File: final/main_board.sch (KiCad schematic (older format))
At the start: 55 parts, among them J1 USB_microB_2040002-1, J2 Arduino_ICSP, J3 Conn_01x15_Male, J4 Conn_01x15_Male, J5 E-INK DISPLAY, J6 BT CONFIG, U1 FT232RL, U2 MCP1702T-5002E_CB, U3 TPS2113ADRBR, U4 ATMEGA328PB-ANR, U5 TXS0108EPW, U6 TXS0104E, U7 RN4871, U8 MCP1702T-3302E/CBCT-ND, U9 TS02CQE, Y1 16MHz

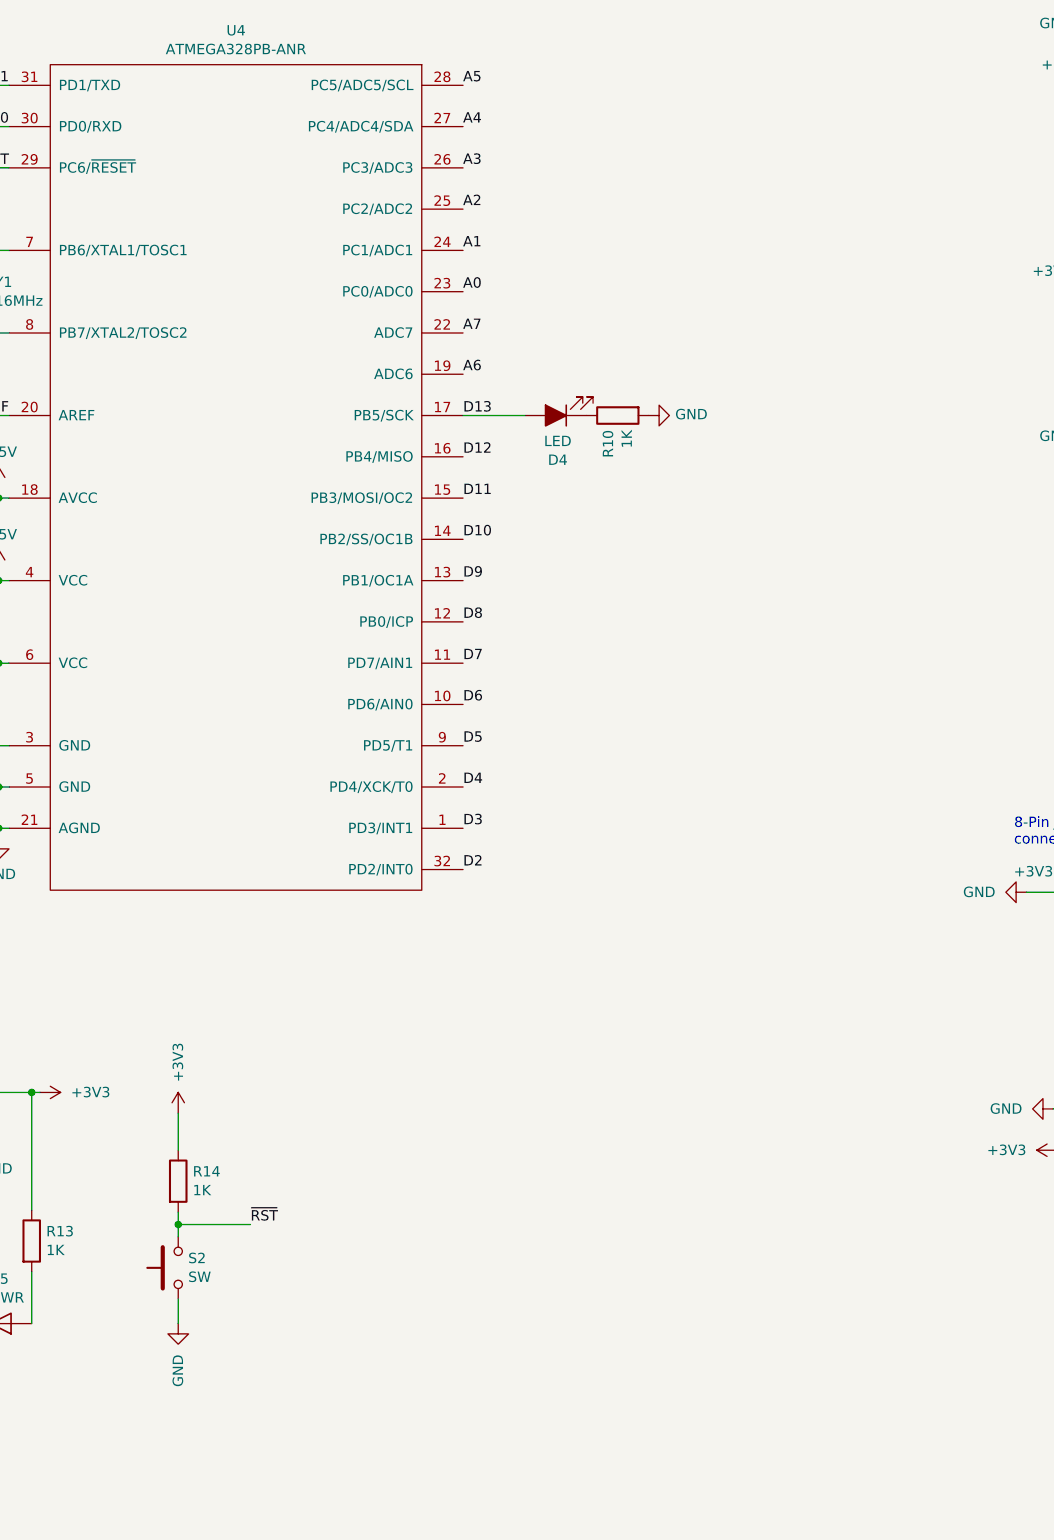
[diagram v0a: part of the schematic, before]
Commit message: Add mode button.
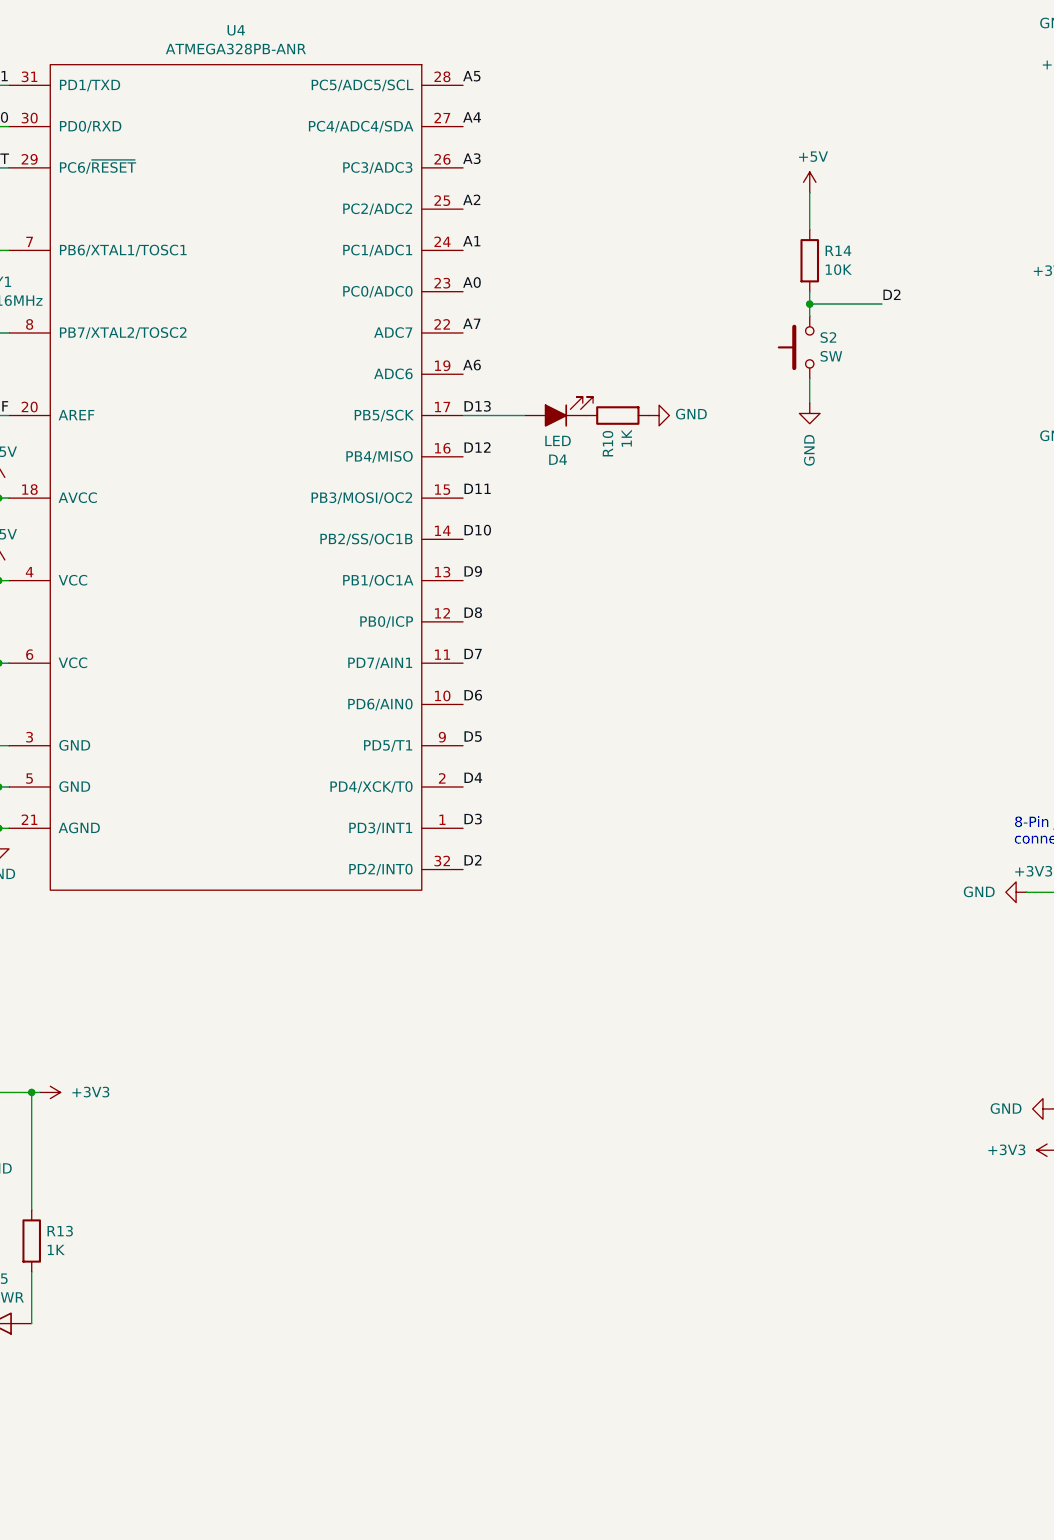
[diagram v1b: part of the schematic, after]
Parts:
- R14: value 1K -> 10K
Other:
- moved on the sheet: R14, S2
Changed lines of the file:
@@
 ~RST
-$Comp
-L power:+3V3 #PWR053
-U 1 1 5CB45D45
-P 9520 9180
-F 0 "#PWR053" H 9520 9030 50  0001 C CNN
-F 1 "+3V3" V 9520 9330 50  0000 L CNN
-F 2 "" H 9520 9180 50  0001 C CNN
-F 3 "" H 9520 9180 50  0001 C CNN
-	1    9520 9180
-	-1   0    0    -1
-$EndComp
 $Comp
 L main_board-rescue:SW-final S2
 U 1 1 5CB4A3A3
-P 9520 9930
-F 0 "S2" H 9568 9976 50  0000 L CNN
-F 1 "SW" H 9568 9885 50  0000 L CNN
-F 2 "Button_Switch_SMD:SW_SPST_B3U-1000P" V 9570 10030 60  0001 C CNN
-F 3 "" V 9570 10030 60  0001 C CNN
-	1    9520 9930
+P 12580 5470
+F 0 "S2" H 12628 5516 50  0000 L CNN
+F 1 "SW" H 12628 5425 50  0000 L CNN
+F 2 "Button_Switch_SMD:SW_SPST_B3U-1000P" V 12630 5570 60  0001 C CNN
+F 3 "" V 12630 5570 60  0001 C CNN
+	1    12580 5470
 	1    0    0    -1
 $EndComp
@@
 L Device:R R14
 U 1 1 5CB4A75B
-P 9520 9510
-F 0 "R14" H 9590 9556 50  0000 L CNN
-F 1 "1K" H 9590 9465 50  0000 L CNN
-F 2 "" V 9450 9510 50  0001 C CNN
-F 3 "~" H 9520 9510 50  0001 C CNN
-	1    9520 9510
+P 12580 5050
+F 0 "R14" H 12650 5096 50  0000 L CNN
+F 1 "10K" H 12650 5005 50  0000 L CNN
+F 2 "" V 12510 5050 50  0001 C CNN
+F 3 "~" H 12580 5050 50  0001 C CNN
+	1    12580 5050
 	1    0    0    -1
 $EndComp
@@
 L power:GND #PWR054
 U 1 1 5CB4A82B
-P 9520 10200
-F 0 "#PWR054" H 9520 9950 50  0001 C CNN
-F 1 "GND" V 9520 10050 50  0000 R CNN
-F 2 "" H 9520 10200 50  0001 C CNN
-F 3 "" H 9520 10200 50  0001 C CNN
-	1    9520 10200
-	1    0    0    -1
-$EndComp
-Wire Wire Line
-	9520 9180 9520 9360
-Wire Wire Line
-	9520 9660 9520 9720
-Wire Wire Line
-	9520 10080 9520 10200
-Text Label 9870 9720 0    50   ~ 0
-~RST
-Wire Wire Line
-	9870 9720 9520 9720
-Connection ~ 9520 9720
-Wire Wire Line
-	9520 9720 9520 9780
+P 12580 5740
+F 0 "#PWR054" H 12580 5490 50  0001 C CNN
+F 1 "GND" V 12580 5590 50  0000 R CNN
+F 2 "" H 12580 5740 50  0001 C CNN
+F 3 "" H 12580 5740 50  0001 C CNN
+	1    12580 5740
+	1    0    0    -1
+$EndComp
+Wire Wire Line
+	12580 4720 12580 4900
+Wire Wire Line
+	12580 5200 12580 5260
+Wire Wire Line
+	12580 5620 12580 5740
+Text Label 12930 5260 0    50   ~ 0
+D2
+Wire Wire Line
+	12930 5260 12580 5260
+Connection ~ 12580 5260
+Wire Wire Line
+	12580 5260 12580 5320
 $Comp
 L Connector:Conn_01x08_Male J6
@@
 Connection ~ 11750 1950
 NoConn ~ 11150 2150
+$Comp
+L power:+5V #PWR?
+U 1 1 5CAC5114
+P 12580 4720
+F 0 "#PWR?" H 12580 4570 50  0001 C CNN
+F 1 "+5V" H 12595 4893 50  0000 C CNN
+F 2 "" H 12580 4720 50  0001 C CNN
+F 3 "" H 12580 4720 50  0001 C CNN
+	1    12580 4720
+	1    0    0    -1
+$EndComp
 $EndSCHEMATC

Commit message: Add diode to 3V3 output of FTDI and power display from Lin Reg.
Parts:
- added D6: D_Schottky, symbol Device:D_Schottky
- added R15: 1K, symbol Device:R
- added S3: SW, Button_Switch_SMD:SW_SPST_B3U-1000P, symbol main_board-rescue:SW-final
- R14: value 10K -> 1K
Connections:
- wire segments 154 -> 159
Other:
- moved on the sheet: R14, S2
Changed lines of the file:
@@
 L power:+3V3 #PWR03
 U 1 1 5C4E2E65
-P 3300 6800
-F 0 "#PWR03" H 3300 6650 50  0001 C CNN
-F 1 "+3V3" V 3315 6928 50  0000 L CNN
-F 2 "" H 3300 6800 50  0001 C CNN
-F 3 "" H 3300 6800 50  0001 C CNN
-	1    3300 6800
+P 3000 6800
+F 0 "#PWR03" H 3000 6650 50  0001 C CNN
+F 1 "+3V3" V 3015 6928 50  0000 L CNN
+F 2 "" H 3000 6800 50  0001 C CNN
+F 3 "" H 3000 6800 50  0001 C CNN
+	1    3000 6800
 	0    -1   -1   0
 $EndComp
@@
 Text Label 14200 5000 2    50   ~ 0
 AREF
-$Comp
-L power:+3V3 #PWR035
-U 1 1 5C5A4A29
-P 13910 8010
-F 0 "#PWR035" H 13910 7860 50  0001 C CNN
-F 1 "+3V3" V 13910 8160 50  0000 L CNN
-F 2 "" H 13910 8010 50  0001 C CNN
-F 3 "" H 13910 8010 50  0001 C CNN
-	1    13910 8010
-	0    -1   1    0
-$EndComp
 Wire Wire Line
 	14000 5100 14200 5100
@@
 	7620 10600 7620 10680
 $Comp
-L power:+3V3 #PWR052
-U 1 1 5CB03E2A
-P 8850 9080
-F 0 "#PWR052" H 8850 8930 50  0001 C CNN
-F 1 "+3V3" V 8850 9230 50  0000 L CNN
-F 2 "" H 8850 9080 50  0001 C CNN
-F 3 "" H 8850 9080 50  0001 C CNN
-	1    8850 9080
-	0    1    -1   0
-$EndComp
-$Comp
 L Device:C C16
 U 1 1 5CB043D0
@@
 L main_board-rescue:SW-final S2
 U 1 1 5CB4A3A3
-P 12580 5470
-F 0 "S2" H 12628 5516 50  0000 L CNN
-F 1 "SW" H 12628 5425 50  0000 L CNN
-F 2 "Button_Switch_SMD:SW_SPST_B3U-1000P" V 12630 5570 60  0001 C CNN
-F 3 "" V 12630 5570 60  0001 C CNN
-	1    12580 5470
+P 9520 9930
+F 0 "S2" H 9568 9976 50  0000 L CNN
+F 1 "SW" H 9568 9885 50  0000 L CNN
+F 2 "Button_Switch_SMD:SW_SPST_B3U-1000P" V 9570 10030 60  0001 C CNN
+F 3 "" V 9570 10030 60  0001 C CNN
+	1    9520 9930
 	1    0    0    -1
 $EndComp
@@
 L Device:R R14
 U 1 1 5CB4A75B
-P 12580 5050
-F 0 "R14" H 12650 5096 50  0000 L CNN
-F 1 "10K" H 12650 5005 50  0000 L CNN
-F 2 "" V 12510 5050 50  0001 C CNN
-F 3 "~" H 12580 5050 50  0001 C CNN
-	1    12580 5050
+P 9520 9510
+F 0 "R14" H 9590 9556 50  0000 L CNN
+F 1 "1K" H 9590 9465 50  0000 L CNN
+F 2 "" V 9450 9510 50  0001 C CNN
+F 3 "~" H 9520 9510 50  0001 C CNN
+	1    9520 9510
 	1    0    0    -1
 $EndComp
@@
 L power:GND #PWR054
 U 1 1 5CB4A82B
-P 12580 5740
-F 0 "#PWR054" H 12580 5490 50  0001 C CNN
-F 1 "GND" V 12580 5590 50  0000 R CNN
-F 2 "" H 12580 5740 50  0001 C CNN
-F 3 "" H 12580 5740 50  0001 C CNN
-	1    12580 5740
-	1    0    0    -1
-$EndComp
-Wire Wire Line
-	12580 4720 12580 4900
-Wire Wire Line
-	12580 5200 12580 5260
-Wire Wire Line
-	12580 5620 12580 5740
-Text Label 12930 5260 0    50   ~ 0
-D2
-Wire Wire Line
-	12930 5260 12580 5260
-Connection ~ 12580 5260
-Wire Wire Line
-	12580 5260 12580 5320
+P 9520 10200
+F 0 "#PWR054" H 9520 9950 50  0001 C CNN
+F 1 "GND" V 9520 10050 50  0000 R CNN
+F 2 "" H 9520 10200 50  0001 C CNN
+F 3 "" H 9520 10200 50  0001 C CNN
+	1    9520 10200
+	1    0    0    -1
+$EndComp
+Wire Wire Line
+	9520 9180 9520 9360
+Wire Wire Line
+	9520 9660 9520 9720
+Wire Wire Line
+	9520 10080 9520 10200
+Text Label 9870 9720 0    50   ~ 0
+~RST
+Wire Wire Line
+	9870 9720 9520 9720
+Connection ~ 9520 9720
+Wire Wire Line
+	9520 9720 9520 9780
 $Comp
 L Connector:Conn_01x08_Male J6
@@
 	1    13760 9160
 	0    1    1    0
-$EndComp
-$Comp
-L power:+3V3 #PWR057
-U 1 1 5CB617A3
-P 13780 9360
-F 0 "#PWR057" H 13780 9210 50  0001 C CNN
-F 1 "+3V3" V 13780 9510 50  0000 L CNN
-F 2 "" H 13780 9360 50  0001 C CNN
-F 3 "" H 13780 9360 50  0001 C CNN
-	1    13780 9360
-	0    -1   1    0
 $EndComp
 Text Label 14190 9260 2    50   ~ 0
@@
 NoConn ~ 6140 10180
 NoConn ~ 6140 10280
-$Comp
-L power:+3V3 #PWR046
-U 1 1 5CADBD7A
-P 5790 8950
-F 0 "#PWR046" H 5790 8800 50  0001 C CNN
-F 1 "+3V3" V 5790 9100 50  0000 L CNN
-F 2 "" H 5790 8950 50  0001 C CNN
-F 3 "" H 5790 8950 50  0001 C CNN
-	1    5790 8950
-	-1   0    0    -1
-$EndComp
 $Comp
 L power:+5V #PWR045
@@
 NoConn ~ 11150 2150
 $Comp
-L power:+5V #PWR?
-U 1 1 5CAC5114
-P 12580 4720
-F 0 "#PWR?" H 12580 4570 50  0001 C CNN
-F 1 "+5V" H 12595 4893 50  0000 C CNN
-F 2 "" H 12580 4720 50  0001 C CNN
-F 3 "" H 12580 4720 50  0001 C CNN
-	1    12580 4720
-	1    0    0    -1
+L power:+3V3 #PWR053
+U 1 1 5CB45D45
+P 9520 9180
+F 0 "#PWR053" H 9520 9030 50  0001 C CNN
+F 1 "+3V3" V 9520 9330 50  0000 L CNN
+F 2 "" H 9520 9180 50  0001 C CNN
+F 3 "" H 9520 9180 50  0001 C CNN
+	1    9520 9180
+	-1   0    0    -1
+$EndComp
+$Comp
+L Device:R R15
+U 1 1 5CACCC33
+P 11120 9420
+F 0 "R15" H 11190 9466 50  0000 L CNN
+F 1 "1K" H 11190 9375 50  0000 L CNN
+F 2 "" V 11050 9420 50  0001 C CNN
+F 3 "~" H 11120 9420 50  0001 C CNN
+	1    11120 9420
+	1    0    0    -1
+$EndComp
+$Comp
+L main_board-rescue:SW-final S3
+U 1 1 5CACCCF1
+P 11120 9840
+F 0 "S3" H 11168 9886 50  0000 L CNN
+F 1 "SW" H 11168 9795 50  0000 L CNN
+F 2 "Button_Switch_SMD:SW_SPST_B3U-1000P" V 11170 9940 60  0001 C CNN
+F 3 "" V 11170 9940 60  0001 C CNN
+	1    11120 9840
+	1    0    0    -1
+$EndComp
+$Comp
+L power:GND #PWR063
+U 1 1 5CACCDD9
+P 11120 10150
+F 0 "#PWR063" H 11120 9900 50  0001 C CNN
+F 1 "GND" V 11120 10000 50  0000 R CNN
+F 2 "" H 11120 10150 50  0001 C CNN
+F 3 "" H 11120 10150 50  0001 C CNN
+	1    11120 10150
+	1    0    0    -1
+$EndComp
+$Comp
+L power:+5V #PWR062
+U 1 1 5CACCF01
+P 11120 9170
+F 0 "#PWR062" H 11120 9020 50  0001 C CNN
+F 1 "+5V" H 11135 9343 50  0000 C CNN
+F 2 "" H 11120 9170 50  0001 C CNN
+F 3 "" H 11120 9170 50  0001 C CNN
+	1    11120 9170
+	1    0    0    -1
+$EndComp
+Text Label 11470 9600 0    50   ~ 0
+D2
+Wire Wire Line
+	11120 9170 11120 9270
+Wire Wire Line
+	11120 9570 11120 9600
+Wire Wire Line
+	11120 9990 11120 10150
+Wire Wire Line
+	11470 9600 11120 9600
+Connection ~ 11120 9600
+Wire Wire Line
+	11120 9600 11120 9690
+$Comp
+L Device:D_Schottky D6
+U 1 1 5CAE88E7
+P 3150 6800
+F 0 "D6" H 3150 7016 50  0000 C CNN
+F 1 "D_Schottky" H 3150 6925 50  0000 C CNN
+F 2 "" H 3150 6800 50  0001 C CNN
+F 3 "~" H 3150 6800 50  0001 C CNN
+	1    3150 6800
+	1    0    0    -1
+$EndComp
+$Comp
+L power:+3.3V #PWR035
+U 1 1 5CAE9E09
+P 5790 8950
+F 0 "#PWR035" H 5790 8800 50  0001 C CNN
+F 1 "+3.3V" V 5805 9078 50  0000 L CNN
+F 2 "" H 5790 8950 50  0001 C CNN
+F 3 "" H 5790 8950 50  0001 C CNN
+	1    5790 8950
+	1    0    0    -1
+$EndComp
+$Comp
+L power:+3.3V #PWR046
+U 1 1 5CAEA2E1
+P 8850 9080
+F 0 "#PWR046" H 8850 8930 50  0001 C CNN
+F 1 "+3.3V" V 8865 9208 50  0000 L CNN
+F 2 "" H 8850 9080 50  0001 C CNN
+F 3 "" H 8850 9080 50  0001 C CNN
+	1    8850 9080
+	0    1    1    0
+$EndComp
+$Comp
+L power:+3.3V #PWR052
+U 1 1 5CAEA6D6
+P 13780 9360
+F 0 "#PWR052" H 13780 9210 50  0001 C CNN
+F 1 "+3.3V" V 13795 9488 50  0000 L CNN
+F 2 "" H 13780 9360 50  0001 C CNN
+F 3 "" H 13780 9360 50  0001 C CNN
+	1    13780 9360
+	0    -1   -1   0
+$EndComp
+$Comp
+L power:+3.3V #PWR057
+U 1 1 5CAEAE36
+P 13910 8010
+F 0 "#PWR057" H 13910 7860 50  0001 C CNN
+F 1 "+3.3V" V 13925 8138 50  0000 L CNN
+F 2 "" H 13910 8010 50  0001 C CNN
+F 3 "" H 13910 8010 50  0001 C CNN
+	1    13910 8010
+	0    -1   -1   0
 $EndComp
 $EndSCHEMATC

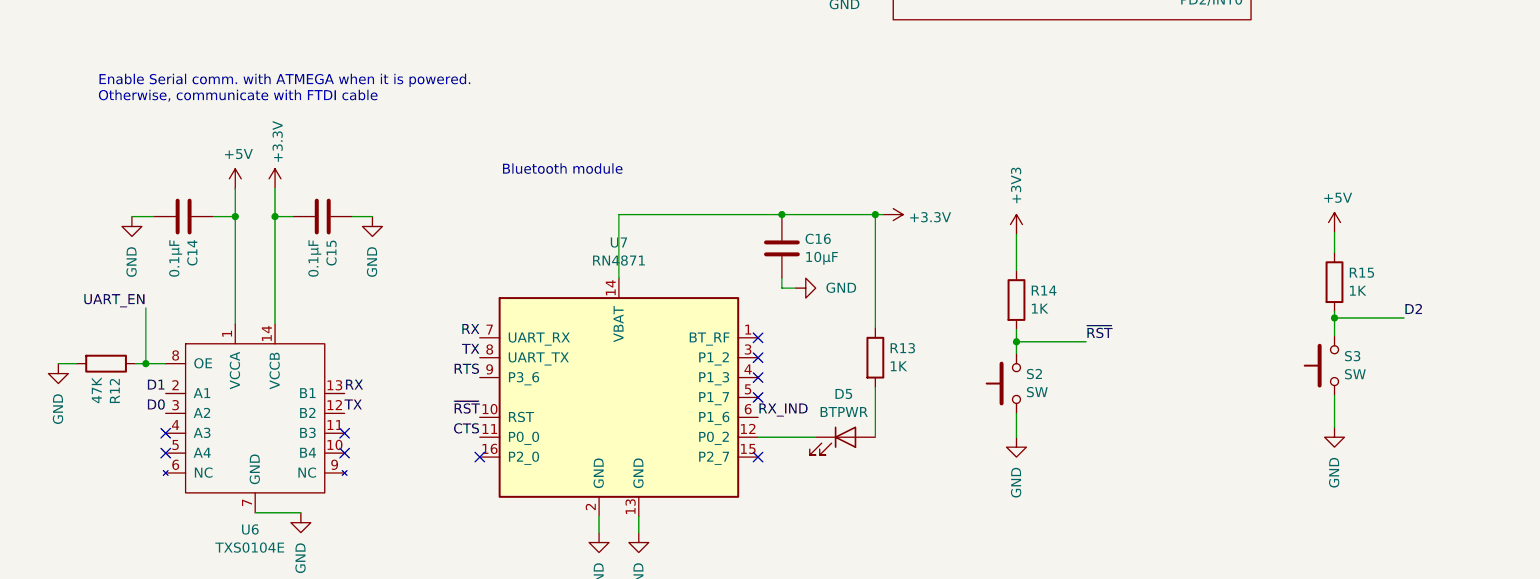
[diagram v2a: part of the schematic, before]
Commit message: Hook up reset on BT to MCU
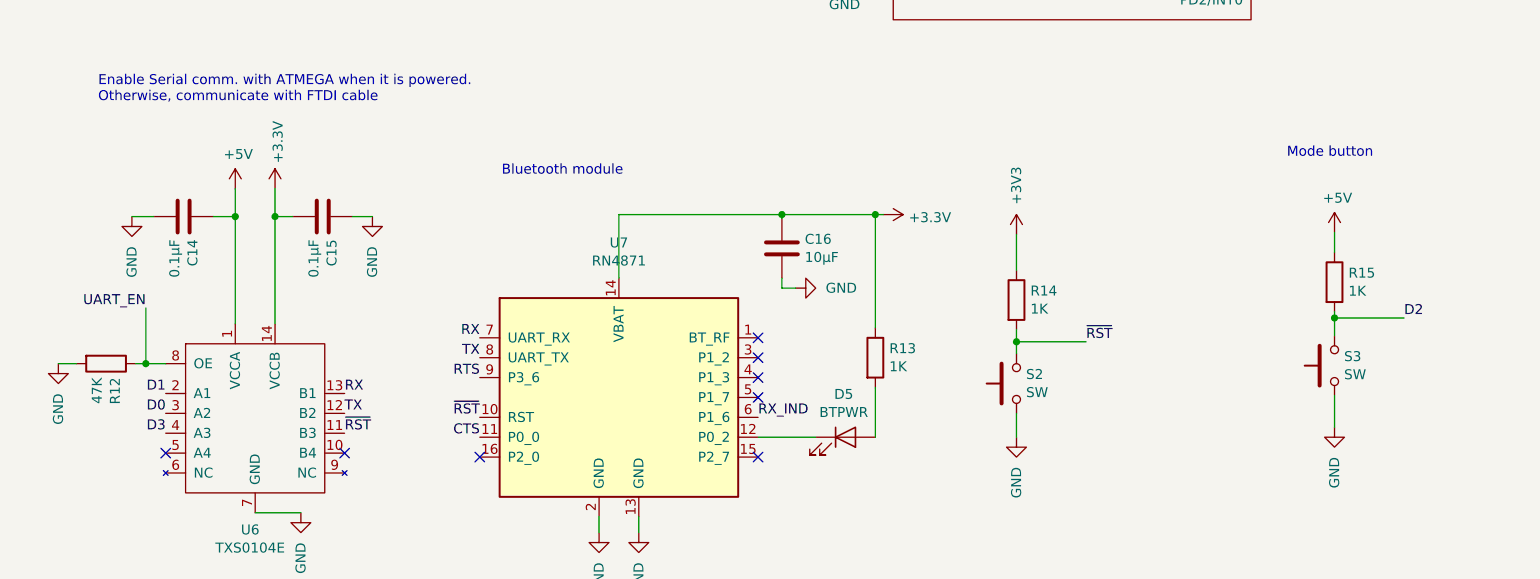
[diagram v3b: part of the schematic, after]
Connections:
- no-connect marks 36 -> 34
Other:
- note added: "Mode button\n"
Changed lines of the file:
@@
 Wire Wire Line
 	5140 9830 5240 9830
-NoConn ~ 5240 10180
 NoConn ~ 5240 10280
-NoConn ~ 6140 10180
 NoConn ~ 6140 10280
 $Comp
@@
 	0    -1   -1   0
 $EndComp
+Text Notes 10880 8800 0    50   ~ 0
+Mode button\n
+Text Label 5240 10180 2    50   ~ 0
+D3
+Text Label 6140 10180 0    50   ~ 0
+~RST
 $EndSCHEMATC

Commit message: Added Power Schematic
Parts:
- removed D6: D_Schottky, symbol Device:D_Schottky
- removed R15: 1K, symbol Device:R
- removed S3: SW, Button_Switch_SMD:SW_SPST_B3U-1000P, symbol main_board-rescue:SW-final
- added C? (x2): 10µF, Capacitor_SMD:C_0603_1608Metric, symbol Device:C
- added C? (x2): 1µF, Capacitor_SMD:C_0603_1608Metric, symbol Device:C
- added D?: LED, LED_SMD:LED_0805_2012Metric, symbol Device:LED_ALT
- added R?: 590, Resistor_SMD:R_0603_1608Metric, symbol Device:R
- added R?: 1.1k, Resistor_SMD:R_0603_1608Metric, symbol Device:R
- added R?: 100k, Resistor_SMD:R_0603_1608Metric, symbol Device:R
- added R? (x3): 10k, Resistor_SMD:R_0603_1608Metric, symbol Device:R
- added R?: 1K, Resistor_SMD:R_0603_1608Metric, symbol Device:R
- added R?: .01, Resistor_SMD:R_0603_1608Metric, symbol Device:R
- added R? (x2): 4.7k, Resistor_SMD:R_0603_1608Metric, symbol Device:R
- added U?: BQ24075, symbol Battery_Management:BQ24075
- added U?: BQ27441-G1, Package_SON:Texas_S-PDSO-N12, symbol Battery_Management:BQ27441-G1
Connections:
- net labels added: BATTERY, OUT, VPU, V_BATT
- wire segments 159 -> 224
- no-connect marks 34 -> 42
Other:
- note removed: "Mode button\n"
- moved on the sheet: C1, C10, C11, C12, C13, C14, C15, C16, C17, C18, C2, C3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
